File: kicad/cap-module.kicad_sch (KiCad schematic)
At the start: 1 part, among them U1 RaspberryPi_Pico

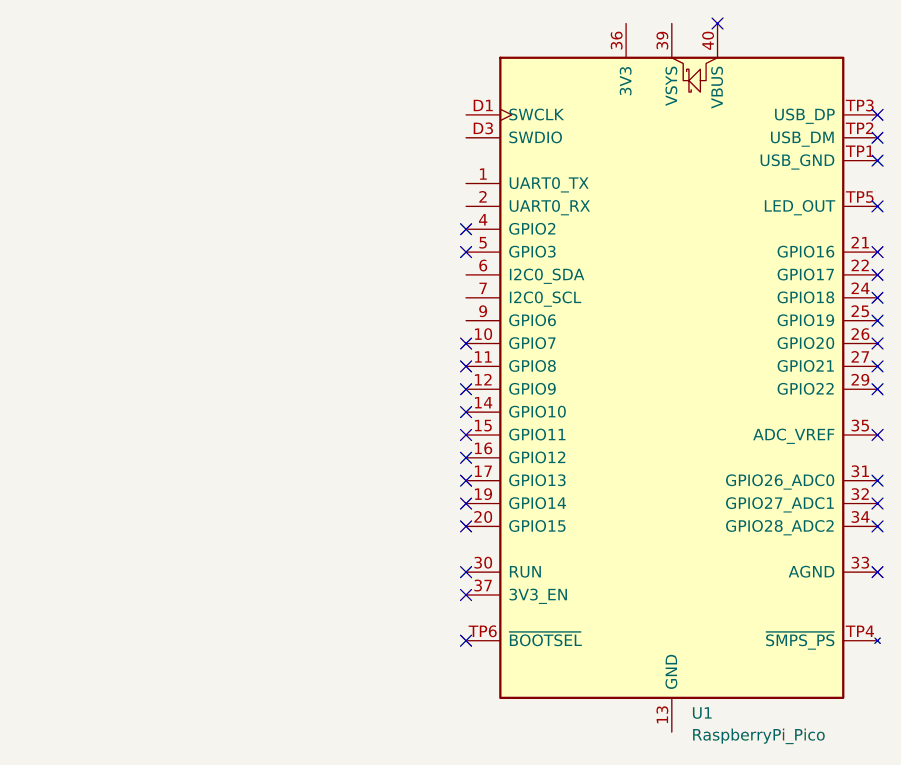
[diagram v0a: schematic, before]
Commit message: Add AD7747
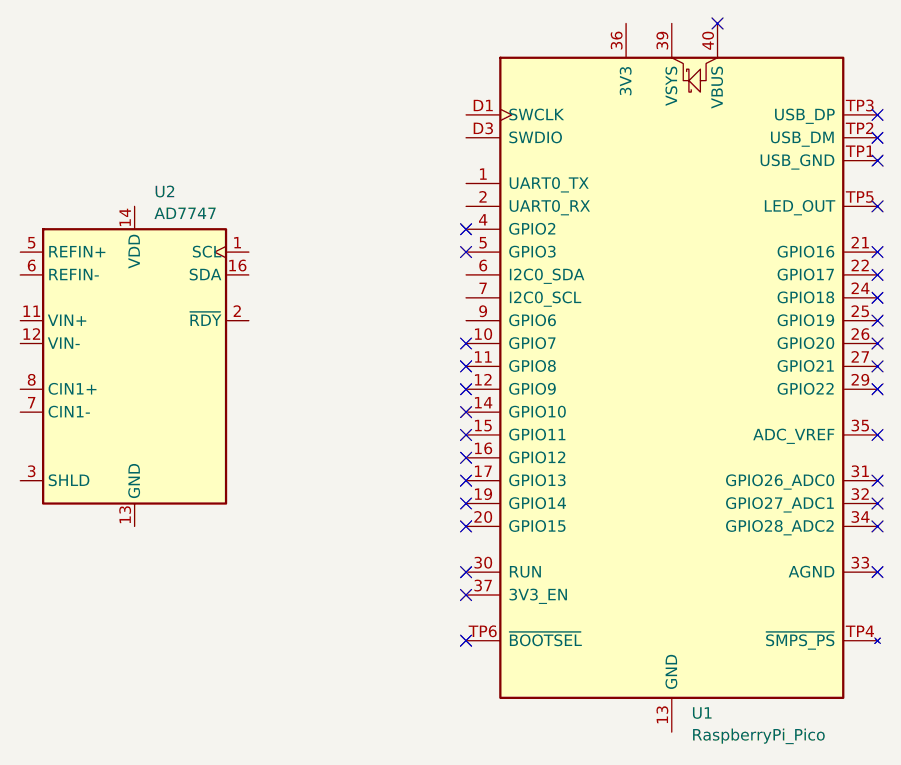
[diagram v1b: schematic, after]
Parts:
- added U2: AD7747, Package_SO:TSSOP-16_4.4x5mm_P0.65mm, symbol Analog_ADC_AD7747:AD7747
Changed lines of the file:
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@@
   (no_connect (at 172.72 100.33))
   (no_connect (at 172.72 90.17))
+  (symbol (lib_id "Analog_ADC_AD7747:AD7747") (at 90.17 97.79 0) (unit 1)
+    (in_bom yes) (on_board yes) (dnp no) (fields_autoplaced)
+    (property "Reference" "U2" (at 92.3641 78.4057 0)
+      (effects (font (size 1.27 1.27)) (justify left))
+    )
+    (property "Value" "AD7747" (at 92.3641 80.8299 0)
+      (effects (font (size 1.27 1.27)) (justify left))
+    )
+    (property "Footprint" "Package_SO:TSSOP-16_4.4x5mm_P0.65mm" (at 90.17 127 0)
+      (effects (font (size 1.27 1.27)) hide)
+    )
+    (property "Datasheet" "https://www.analog.com/media/en/technical-documentation/data-sheets/AD7747.pdf" (at 90.17 129.54 0)
+      (effects (font (size 1.27 1.27)) hide)
+    )
+    (pin "1")
+    (pin "11")
+    (pin "12")
+    (pin "13")
+    (pin "14")
+    (pin "16")
+    (pin "2")
+    (pin "3")
+    (pin "5")
+    (pin "6")
+    (pin "7")
+    (pin "8")
+    (pin "10")
+    (pin "15")
+    (pin "4")
+    (pin "9")
+    (instances
+      (project "cap-module"
+        (path "/2da8fa58-ccef-42b1-8320-baeb3fec91e3"
+          (reference "U2") (unit 1)
+        )
+      )
+    )
+  )
   (symbol (lib_id "MCU_Module_RaspberryPi_Pico:RaspberryPi_Pico_SecondaryPins") (at 149.86 100.33 0) (unit 1)
     (in_bom yes) (on_board yes) (dnp no) (fields_autoplaced)
